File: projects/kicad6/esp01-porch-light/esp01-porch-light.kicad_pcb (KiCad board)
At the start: 2 copper layers, 49.3 x 40.9 mm, 15 parts, among them J1 RELAY, J2 Conn_01x02_Male, Q1 2N3904, U1 AMS1117-3.3, U2 ESP01

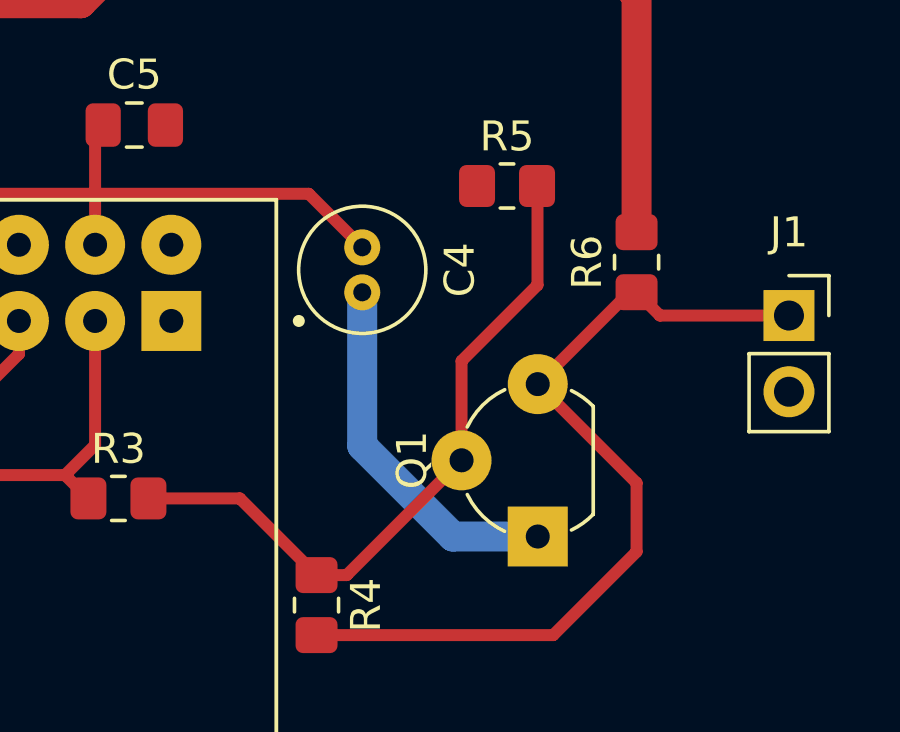
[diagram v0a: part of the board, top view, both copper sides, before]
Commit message: esp01_porch light: fix the GNDing
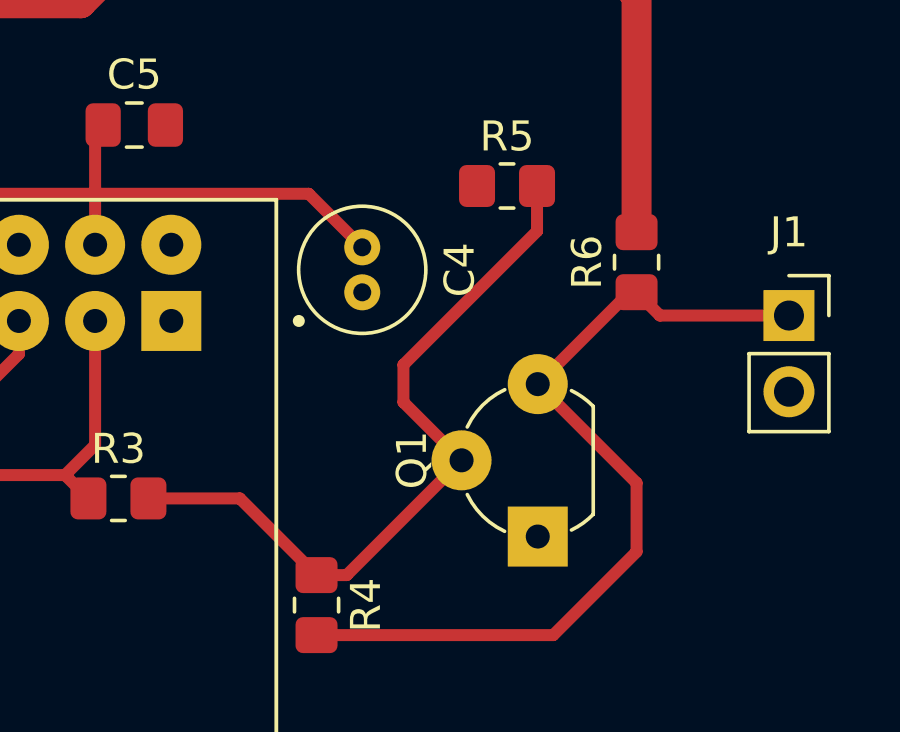
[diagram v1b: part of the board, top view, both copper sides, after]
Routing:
- net GND: track 30.7 -> 18.6 mm
- net Net-(Q1-Pad2): track 23.3 -> 24.9 mm
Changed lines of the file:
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@@
       (effects (font (size 1 1) (thickness 0.15)))
     )
-    (fp_text value "Conn_01x02_Male" (at -0.508 5.842) (layer "F.Fab")
+    (fp_text value "Conn_01x02_Male" (at 3.455 -0.486 90) (layer "F.Fab")
       (effects (font (size 1 1) (thickness 0.15)))
     )
@@
   (segment (start 82.296 118.364) (end 76.962 113.03) (width 1) (layer "B.Cu") (net 2))
   (segment (start 75.946 113.03) (end 70.612 118.364) (width 1) (layer "B.Cu") (net 2))
-  (segment (start 98.052 146.05) (end 95.224263 146.05) (width 1) (layer "B.Cu") (net 2))
-  (segment (start 95.224263 146.05) (end 92.202 143.027737) (width 1) (layer "B.Cu") (net 2))
-  (segment (start 92.202 143.027737) (end 92.202 138.009511) (width 1) (layer "B.Cu") (net 2))
   (segment (start 70.612 118.364) (end 68.834 118.364) (width 1) (layer "B.Cu") (net 2))
   (segment (start 68.834 118.364) (end 68.326 117.856) (width 1) (layer "B.Cu") (net 2))
@@
   (segment (start 101.346 137.906) (end 101.116 137.906) (width 0.4) (layer "F.Cu") (net 4))
   (segment (start 98.568 149.336) (end 101.346 146.558) (width 0.4) (layer "F.Cu") (net 4))
-  (segment (start 95.512 143.51) (end 95.512 140.2) (width 0.4) (layer "F.Cu") (net 5))
+  (segment (start 95.512 143.51) (end 93.575 141.573) (width 0.4) (layer "F.Cu") (net 5))
+  (segment (start 93.575 140.325) (end 98.028 135.872) (width 0.4) (layer "F.Cu") (net 5))
   (segment (start 91.686 147.336) (end 90.678 147.336) (width 0.4) (layer "F.Cu") (net 5))
   (segment (start 98.044 134.382) (end 98.028 134.366) (width 0.4) (layer "F.Cu") (net 5))
-  (segment (start 98.044 137.668) (end 98.044 134.382) (width 0.4) (layer "F.Cu") (net 5))
-  (segment (start 95.512 140.2) (end 98.044 137.668) (width 0.4) (layer "F.Cu") (net 5))
   (segment (start 88.122 144.78) (end 90.678 147.336) (width 0.4) (layer "F.Cu") (net 5))
   (segment (start 85.074 144.78) (end 88.122 144.78) (width 0.4) (layer "F.Cu") (net 5))
+  (segment (start 98.028 135.872) (end 98.028 134.366) (width 0.4) (layer "F.Cu") (net 5))
+  (segment (start 93.575 141.573) (end 93.575 140.325) (width 0.4) (layer "F.Cu") (net 5))
   (segment (start 95.512 143.51) (end 91.686 147.336) (width 0.4) (layer "F.Cu") (net 5))
   (segment (start 80.7575 139.9685) (end 80.7575 138.865) (width 0.4) (layer "F.Cu") (net 6))

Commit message: Add porch light updated schematic
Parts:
- J1: value RELAY -> Relay; footprint Connector_PinSocket_2.54mm:PinSocket_1x02_P2.54mm_Vertical -> Connector_PinSocket_2.54mm:PinSocket_1x03_P2.54mm_Vertical
- J2: value Conn_01x02_Male -> Power_IN
- moved C5 1.49 mm to (84.5, 130.8)
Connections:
- J1 pad 1: RELAY_IN -> +5V
- J1 pad 2: RELAY_IN -> GND
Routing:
- net +5V: track 52.2 -> 63.0 mm
- net 3.3v: track 63.4 -> 64.8 mm

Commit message: update esp 01 port light PCB
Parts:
- removed R4, R5: 10k, Resistor_SMD:R_0805_2012Metric_Pad1.20x1.40mm_HandSolder
- C4: footprint Capacitor_THT:C_Radial_D4.0mm_H7.0mm_P1.50mm -> Capacitor_THT:C_Radial_D10.0mm_H20.0mm_P5.00mm
- J2: value Power_IN -> Conn_01x02_Male
- R2: value 10k -> 1k
- R3: value 1k -> 10k
- moved C4 7.48 mm to (93.2, 129.0)
- moved R1 1.48 mm to (73.8, 138.5)
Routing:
- net RELAY_IN: track 28.6 -> 14.1 mm
- net Net-(Q1-Pad2): track 24.9 -> 11.0 mm
- net GND: track 18.6 -> 14.2 mm
- net GPIO0: track 10.7 -> 9.71 mm
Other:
- board text added: "Porch Light"
